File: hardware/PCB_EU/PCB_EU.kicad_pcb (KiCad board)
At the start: 4 copper layers, 100 x 100 mm, 197 parts, among them J101 24 V IN, J201 UART 3V3, J301 MEM2061 SPI, J401 SHT 3V3 / GND, J402 SHT SDA / SCL, J403 FLOAT / GND, J411 FAN1: GND / +12, J412 FAN1: TACH / PWM, J421 FAN2: GND / +12, J422 FAN2: TACH / PWM, J501 LED1 + / GND, J601 LED2 + / GND, J602 BAR2 + / GND, J701 PTC + / RETURN, J702 PUMP + / RETURN, Q102 IRF1010ESPBF, Q411 FAN1 AO3422, Q421 FAN2 AO3422, Q501 IRF540ZPBF, Q601 IRF540ZPBF, Q701 BC847B-DIO, Q702 BC857B, Q703 IRF1010ESPBF, Q704 AO3422, SW201 RESET, SW202 BOOT, U101 L7987 3A, U201 AP63203WU-7, U202 ESP32-WROOM-32E-N4, U301 MCP7940N-I/SN, U401 USBLC6-2SC6, U402 USBLC6-2SC6, U501 LM3429MH/NOPB, U601 LM3429MH/NOPB, U802 LM2903D-ST, Y301 32.768k CL7p

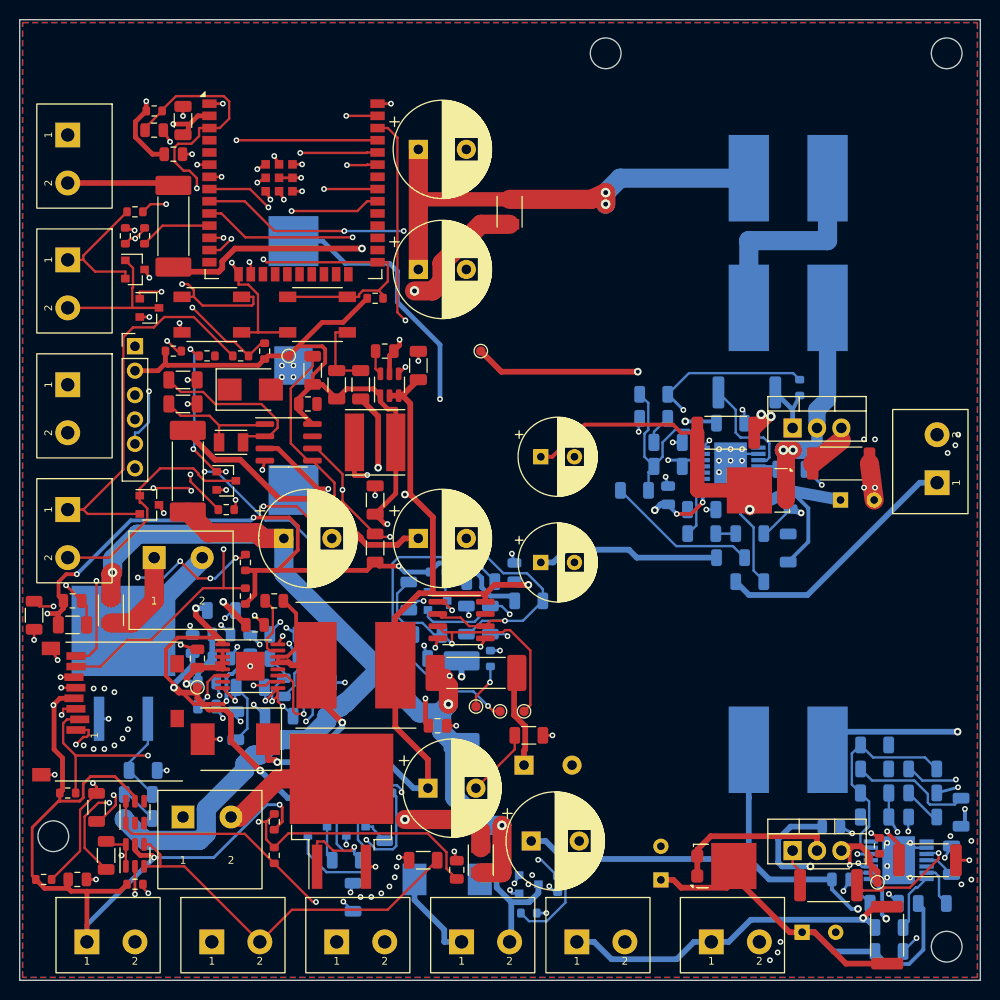
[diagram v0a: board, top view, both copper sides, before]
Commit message: PCB_EU: route the last 13 connections (0 unrouted, DRC 0)
- Hand-planned pin escapes in routing.json for U501/U601 (LM3429) between
  the via-free heatsink reserves, the nine-part block above U601 rearranged
  into five columns, BLOCK_OC at U101.12 and a GND via for R706/Q701.
- D101 moved from under the battery next to F103; R503, C504-C507, C511,
  C604, C611, R807 and R104 nudged. No value, MPN or BOM change.
- route_complete: keep 0.8 mm free in front of fine-pitch IC pins, retry
  failed nets first, then shortest nets first.
- route_board: drop session copper that breaks clearance to planned copper
  and prune the dead ends, so small plan edits do not need a new
  Freerouting run; Freerouting sessions regenerated.
- plot_board: stage label follows the unrouted count.
- Docs and review outputs updated: 1527 tracks / 285 vias, 0 unrouted,
  DRC 0, parity 0; rebuild gives a byte-identical board.

Co-Authored-By: Claude Opus 5.5 (1M context) <noreply@anthropic.com>
Claude-Session: https://claude.ai/code/session_01AxccZX6Cb4FnRKJMrFYMSX
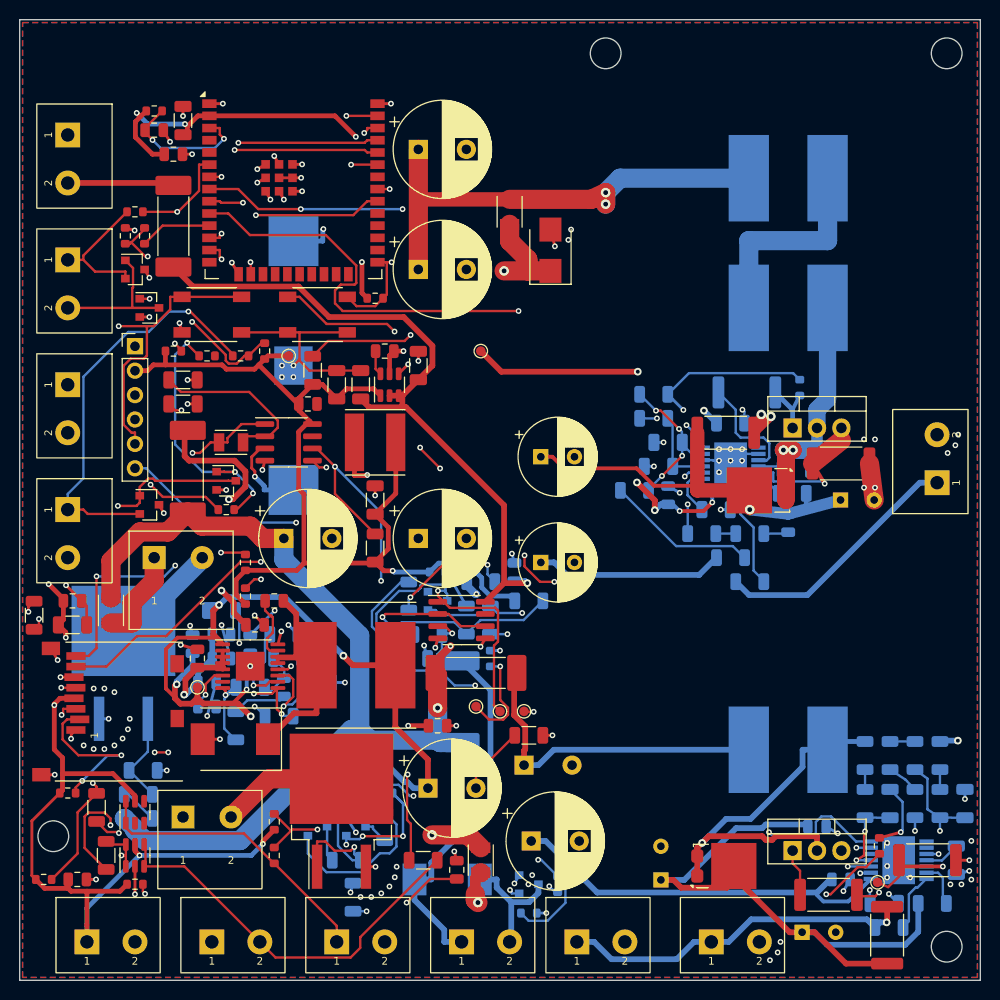
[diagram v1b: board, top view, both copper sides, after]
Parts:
- moved D101 34.5 mm to (55.2, 24.0), turned to 90 degrees
- moved R609 21.1 mm to (95.8, 76.6), turned to -90 degrees
- moved R607 11.6 mm to (88.0, 76.6), turned to -90 degrees
- moved C607 9.46 mm to (98.4, 81.6), turned to 90 degrees
- moved R503 5.71 mm to (80.4, 49.3), turned to 180 degrees
- moved R606 5.17 mm to (90.6, 76.6), turned to 90 degrees
- moved R611 4.34 mm to (93.2, 76.6), turned to 90 degrees
- moved R610 4.02 mm to (95.8, 81.6), turned to -90 degrees
- moved R608 3.74 mm to (88.0, 81.6), turned to -90 degrees
- moved C506 2.69 mm to (66.5, 46.5), turned to 180 degrees
- moved C507 2.50 mm to (67.5, 44.0), turned to 180 degrees
- moved C511 2.41 mm to (80.0, 52.4)
- moved C606 2.13 mm to (90.6, 81.6), turned to 90 degrees
- moved R605 1.61 mm to (93.2, 81.6), turned to 90 degrees
- moved C505 1.50 mm to (72.5, 51.0)
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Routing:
- net LED_NDIM: track 54.3 -> 110.5 mm, vias 3 -> 4
- net LED2_SW: track 75.6 -> 40.1 mm, vias 2 -> 1
- net LED2_OUT: track 67.2 -> 97.0 mm
- net BLOCK_OC: track 31.7 -> 59.5 mm
- net I2C_SDA: track 116.5 -> 141.0 mm, vias 5 -> 4
- net LED2_OVP_MID: track 25.6 -> 2.08 mm, vias 2 -> 0
- net VBAT: track 60.4 -> 41.8 mm
- net PUMP_GPIO: track 98.0 -> 115.6 mm, vias 3 -> 4
- net LED2_GATE: track 3.92 -> 18.4 mm, vias 0 -> 1
- net ESP_BOOT: track 62.5 -> 76.3 mm, vias 1 -> 3
- net AUX_COMP_MID: track 18.3 -> 5.68 mm, vias 2 -> 0
- net UVLO_REF: track 42.6 -> 30.9 mm
- net +3V3: track 308.0 -> 319.0 mm
- net LED2_RT_MID: track 12.8 -> 2.08 mm
- net LED1_IS: track 46.0 -> 56.4 mm, vias 1 -> 2
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
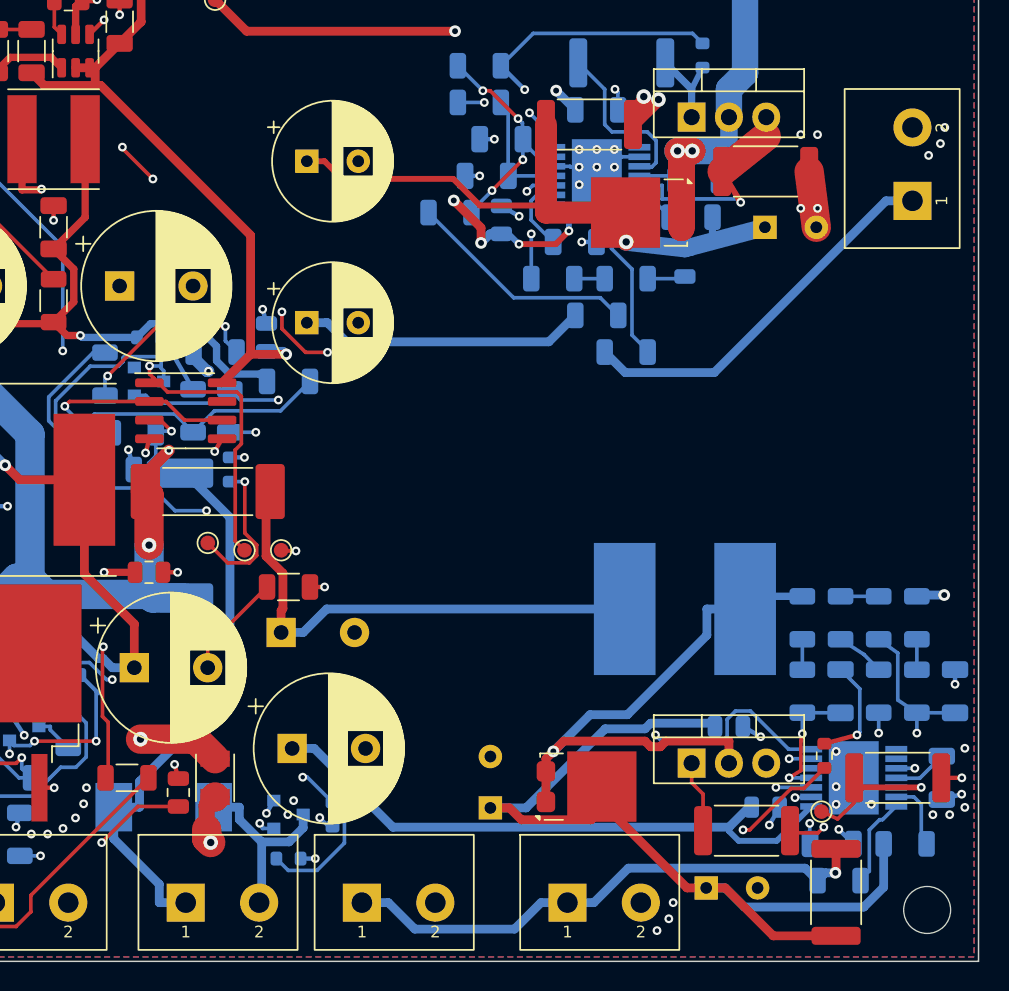
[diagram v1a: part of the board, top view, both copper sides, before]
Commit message: PCB_EU: hand-route LED2 power loop, 5 mm cap footprint, TK22E10N1 switches
- C508-C510, C608, C609 (EEUFR1J101LB) use CP_Radial_D8.0mm_P5.00mm, the
  real 5 mm lead pitch; the 3.5 mm footprint is removed and the 3D fit check
  has no known issues left.
- LED2 is placed and routed like LED1: R601 under Q601, D601 anodes toward
  the switch, C611 between C609 leads, wide SW/IS/OUT/GND copper, LED+ and
  the gate on In2. Eight new connected groups are checked.
- route_board.py drops session copper of nets the plan now routes
  (replace_session_nets) and session vias that break hole spacing, and no
  longer prunes GND stitching vias before the pours exist.
- Q501/Q601: IRF540Z -> Toshiba TK22E10N1 (28 nC instead of 42 nC gate
  charge for the 7 V LM3429 driver); BOM 78.59 -> 77.95 EUR.

0 unrouted, DRC 0, schematic parity 0; rebuild is byte-identical.

Co-Authored-By: Claude Opus 5.5 (1M context) <noreply@anthropic.com>
Claude-Session: https://claude.ai/code/session_01AxccZX6Cb4FnRKJMrFYMSX
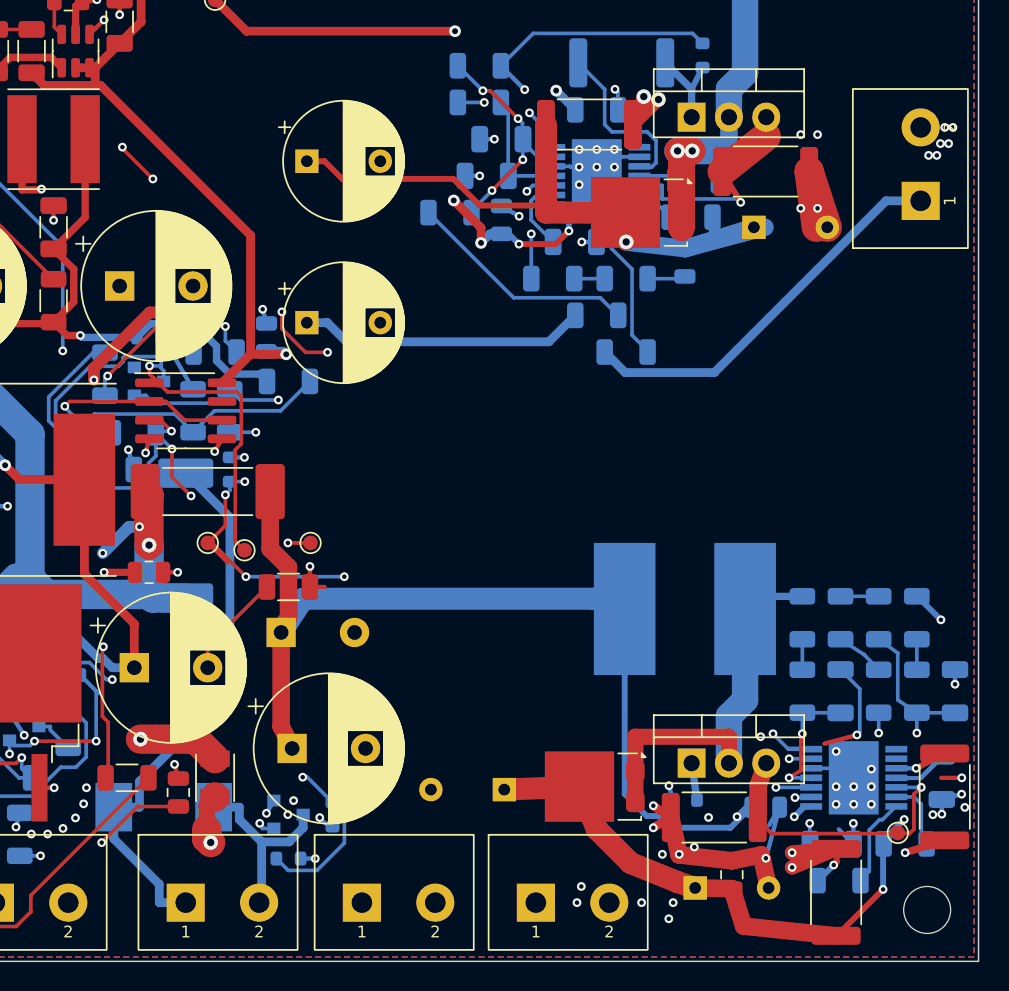
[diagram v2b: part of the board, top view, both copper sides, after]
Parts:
- C508, C509, C510, C608, C609: footprint Capacitor_THT:CP_Radial_D8.0mm_P3.50mm -> Capacitor_THT:CP_Radial_D8.0mm_P5.00mm
- C611: moved to F.Cu
- Q501, Q601: value IRF540ZPBF -> TK22E10N1
- R808: moved to B.Cu
- moved R807 13.7 mm to (97.7, 88.8), turned to -90 degrees
- moved R601 12.8 mm to (82.0, 90.2), turned to 180 degrees
- moved C611 10.1 mm to (83.2, 94.1), turned to 90 degrees
- moved R808 9.96 mm to (80.0, 89.0), turned to 180 degrees
- moved TP08 5.40 mm to (94.5, 91.2)
- moved J602 2.15 mm to (69.8, 96.0)
- moved TP05 2.06 mm to (54.5, 71.5)
- moved C608 1.57 mm to (67.7, 88.3), turned to 180 degrees
- moved C508 0.75 mm to (84.7, 50.0)
- moved C609 0.75 mm to (80.7, 95.0)
- moved D601 0.56 mm to (73.9, 88.1), turned to -90 degrees
- moved J501 0.56 mm to (96.1, 48.2)
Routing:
- net LED2_OUT: track 97.0 -> 54.6 mm, vias 1 -> 3
- net GND: track 166.4 -> 190.8 mm, vias 124 -> 139
- net +24V_FUSED: track 190.0 -> 206.5 mm, vias 5 -> 8
- net LED2_SW: track 40.1 -> 26.1 mm, vias 1 -> 0
- net +24V_LED2: track 83.7 -> 72.5 mm, vias 0 -> 2
- net LED2_LED_POS: track 36.9 -> 47.6 mm, vias 1 -> 3
- net LED2_GATE_RAW: track 11.7 -> 3.55 mm, vias 2 -> 1
- net LED2_GATE: track 18.4 -> 24.8 mm
- net LED2_IS: track 25.5 -> 19.8 mm
- net LED1_OUT: track 73.0 -> 78.0 mm
- net LED2_VCC: track 3.75 -> 7.53 mm
- net LED_NDIM: track 110.5 -> 107.8 mm, vias 4 -> 7
- net LED1_LED_POS: track 56.1 -> 58.8 mm
- net UVLO_SENSE: track 35.4 -> 37.0 mm, vias 3 -> 4

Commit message: PCB_EU: INA226 power monitor in the 24 V return
Adds U102 INA226 (I2C 0x40) with a 5 mOhm low-side shunt (R111 || R112,
2x 0R01 2512) between board GND and the Q102 source (new net RTN_SHUNT).
IN+/IN- are Kelvin tracks; a fill keepout keeps the GND pour off the IN+
track. VBUS is fed from +24V_FUSED through R113 1k with D103 BZV55-C33
so the D101 42 V clamp stays below the 40 V abs max. C115 decouples VS.

Board fully routed again: DRC 0, parity 0, 0 unconnected, rebuild
byte-identical. BOM EUR 82.50 (+4.55). DESIGN.md has the firmware data
(address, shunt, CAL, accuracy) and the new power-monitor section.

Co-Authored-By: Claude Sonnet 5.5 <noreply@anthropic.com>
Claude-Session: https://claude.ai/code/session_01AxccZX6Cb4FnRKJMrFYMSX
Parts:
- added C115: 100n VS, Capacitor_SMD:C_0805_2012Metric, B.Cu at (9.00, 82.0)
- added D103: 33V zener, Diode_SMD:D_MiniMELF, B.Cu at (12.5, 88.2)
- added R111: 0R01 3W 1%, Resistor_SMD:R_2512_6332Metric, B.Cu at (12.2, 77.6)
- added R112: 0R01 3W 1%, Resistor_SMD:R_2512_6332Metric, B.Cu at (4.35, 77.6)
- added R113: 1k VBUS, Resistor_SMD:R_0603_1608Metric, B.Cu at (16.8, 88.2)
- added U102: INA226, Package_SO:VSSOP-10_3x3mm_P0.5mm, B.Cu at (12.0, 83.2)
- moved R108 7.99 mm to (18.9, 78.6)
- moved R109 7.94 mm to (18.9, 76.2), turned to 180 degrees
- moved R110 7.47 mm to (18.9, 73.8)
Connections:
- Q102 pad 3: GND -> RTN_SHUNT
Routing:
- net SD_MOSI_GPIO: track 93.9 -> 146.3 mm, vias 4 -> 8
- net +3V3: track 319.0 -> 363.5 mm, vias 11 -> 23
- net I2C_SCL: track 94.7 -> 135.8 mm, vias 4 -> 5
- net GND: track 190.8 -> 214.4 mm, vias 139 -> 150
- net +24V_FUSED: track 206.5 -> 219.8 mm, vias 8 -> 9
- net RTN_SHUNT: track 0.00 -> 13.1 mm
- net INA_VBUS: track 0.00 -> 10.8 mm
- net +12V: track 212.3 -> 204.6 mm, vias 6 -> 7
- net SD_CS: track 75.4 -> 80.3 mm, vias 3 -> 4
- net SD_MOSI: track 22.6 -> 27.2 mm
- net AUX_SS: track 4.80 -> 8.73 mm
- net FLOAT_GPIO: track 122.5 -> 125.4 mm, vias 3 -> 9
- net REVP_GATE: track 9.69 -> 7.54 mm
- net SHT_SDA: track 18.8 -> 20.5 mm, vias 1 -> 0
- net REVP_MID: track 3.96 -> 2.40 mm
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
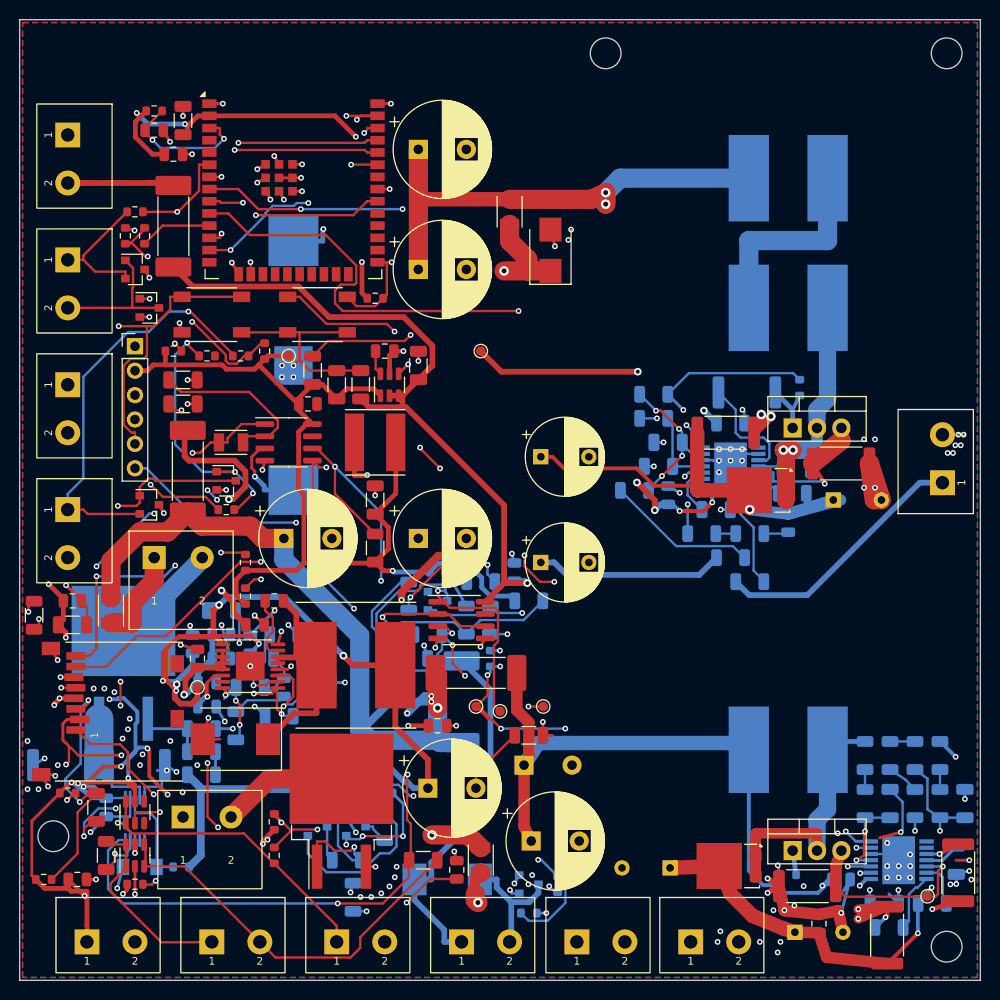
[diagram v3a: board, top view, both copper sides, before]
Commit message: PCB_EU: rework 24 V power copper for standard 1 oz
Widen and duplicate the high-current copper instead of ordering 2 oz:
+24V_RAW 3.0 mm F, PSU_RTN 4.5 mm B, the F101.2 -> C101.1 trunk as F 2.0 mm
plus B 2.5 mm joined by 12 vias, C101.1 hub branch 3.0 mm B, PTC feed 1.5 mm F,
PTC leg and LED1 feed 2.0 mm F/B. The PTC and LED branches leave In2.
BLOCK_OC gets a hand-planned detour around the new feed.

DRC 0, schematic parity 0, 0 unconnected, rebuild byte-identical. Worst
IPC-2221 rise is 54 C on a short neck at F101.1; the rest is 38 C or less.
ampacity.py now joins vias and pads by overlap and scales via resistance by
drill. DESIGN.md and README carry the before/after table.

Co-Authored-By: Claude Sonnet 5.5 <noreply@anthropic.com>
Claude-Session: https://claude.ai/code/session_01AxccZX6Cb4FnRKJMrFYMSX
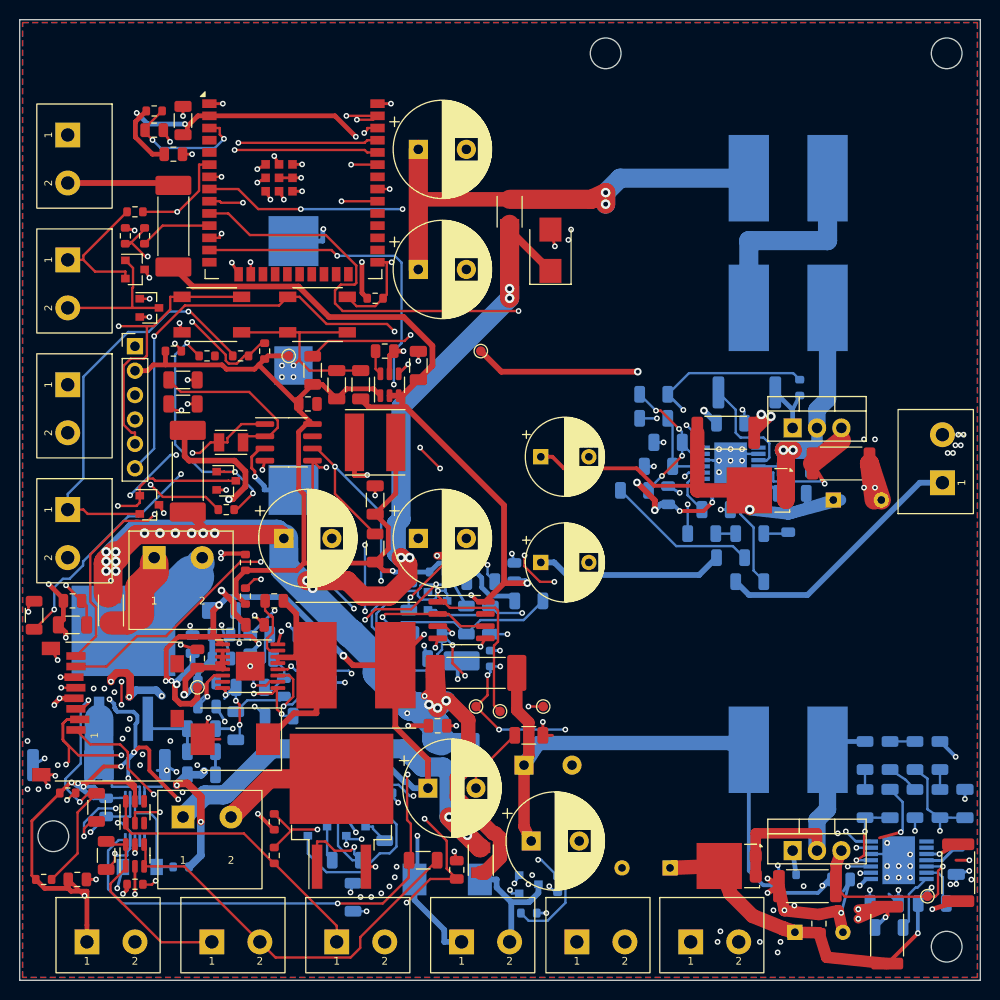
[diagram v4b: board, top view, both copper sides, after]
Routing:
- net +24V_FUSED: track 219.8 -> 249.4 mm, vias 9 -> 33
- net ESP_BOOT: track 76.3 -> 60.0 mm
- net +12V: track 204.6 -> 189.2 mm, vias 7 -> 9
- net SD_MOSI_GPIO: track 146.3 -> 135.2 mm
- net SD_DAT1: track 27.5 -> 36.6 mm
- net +24V_PTC: track 34.8 -> 43.6 mm, vias 1 -> 3
- net +3V3: track 363.5 -> 357.5 mm, vias 23 -> 22
- net BLOCK_OC: track 59.5 -> 64.2 mm, vias 2 -> 5
- net PTC_NPN_B: track 23.6 -> 19.1 mm
- net FLOAT_GPIO: track 125.4 -> 120.9 mm, vias 9 -> 7
- net SD_SCK_GPIO: track 66.4 -> 62.7 mm, vias 2 -> 3
- net +24V_PUMP: track 37.9 -> 34.5 mm, vias 0 -> 2
- net LED_NDIM: track 107.8 -> 105.9 mm
- net +24V_RAW: track 9.95 -> 9.25 mm
